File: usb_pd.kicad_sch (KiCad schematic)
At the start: 41 parts, among them J1 USB-C_GCT_USB4105-GF-A, J2 JST_SH_1x4_SM04B-SRSS-TB-LF-SN, Q1 SQS401EN-T1_BE3, U1 STUSB4500_QFN, U5 TVS2200DRVR, U6 TPD4E02B04DQA, U7 TVS2200DRVR, U8 TVS2200DRVR

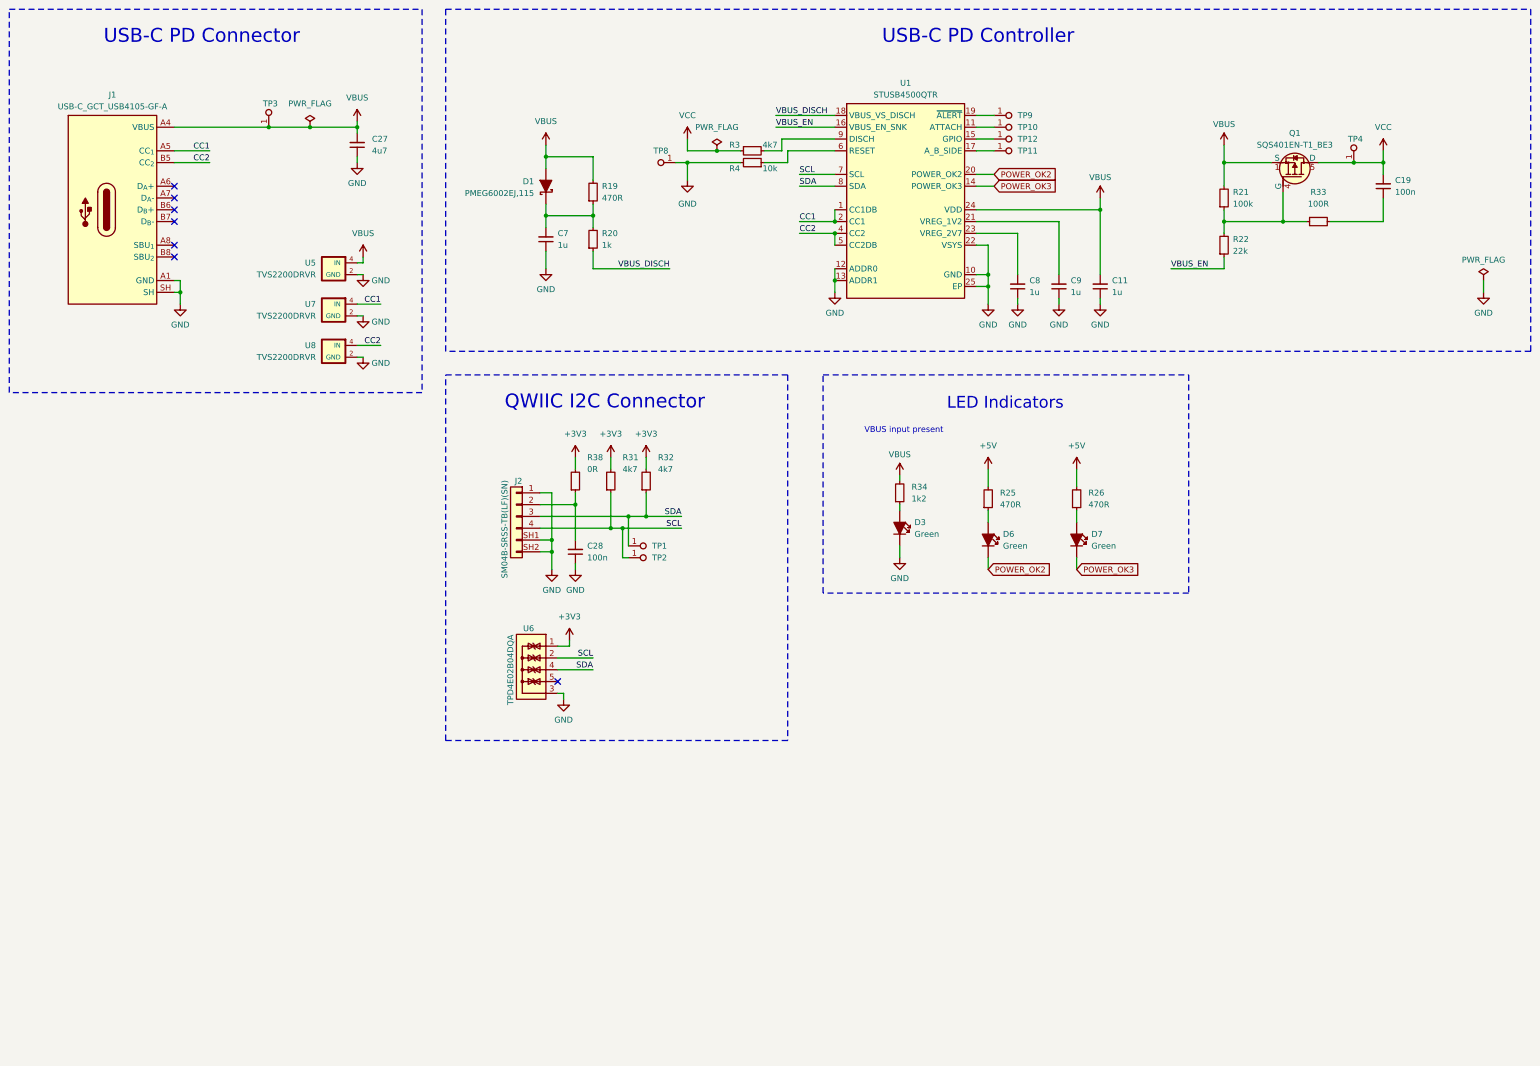
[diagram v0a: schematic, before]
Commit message: [#57225] Finish placement
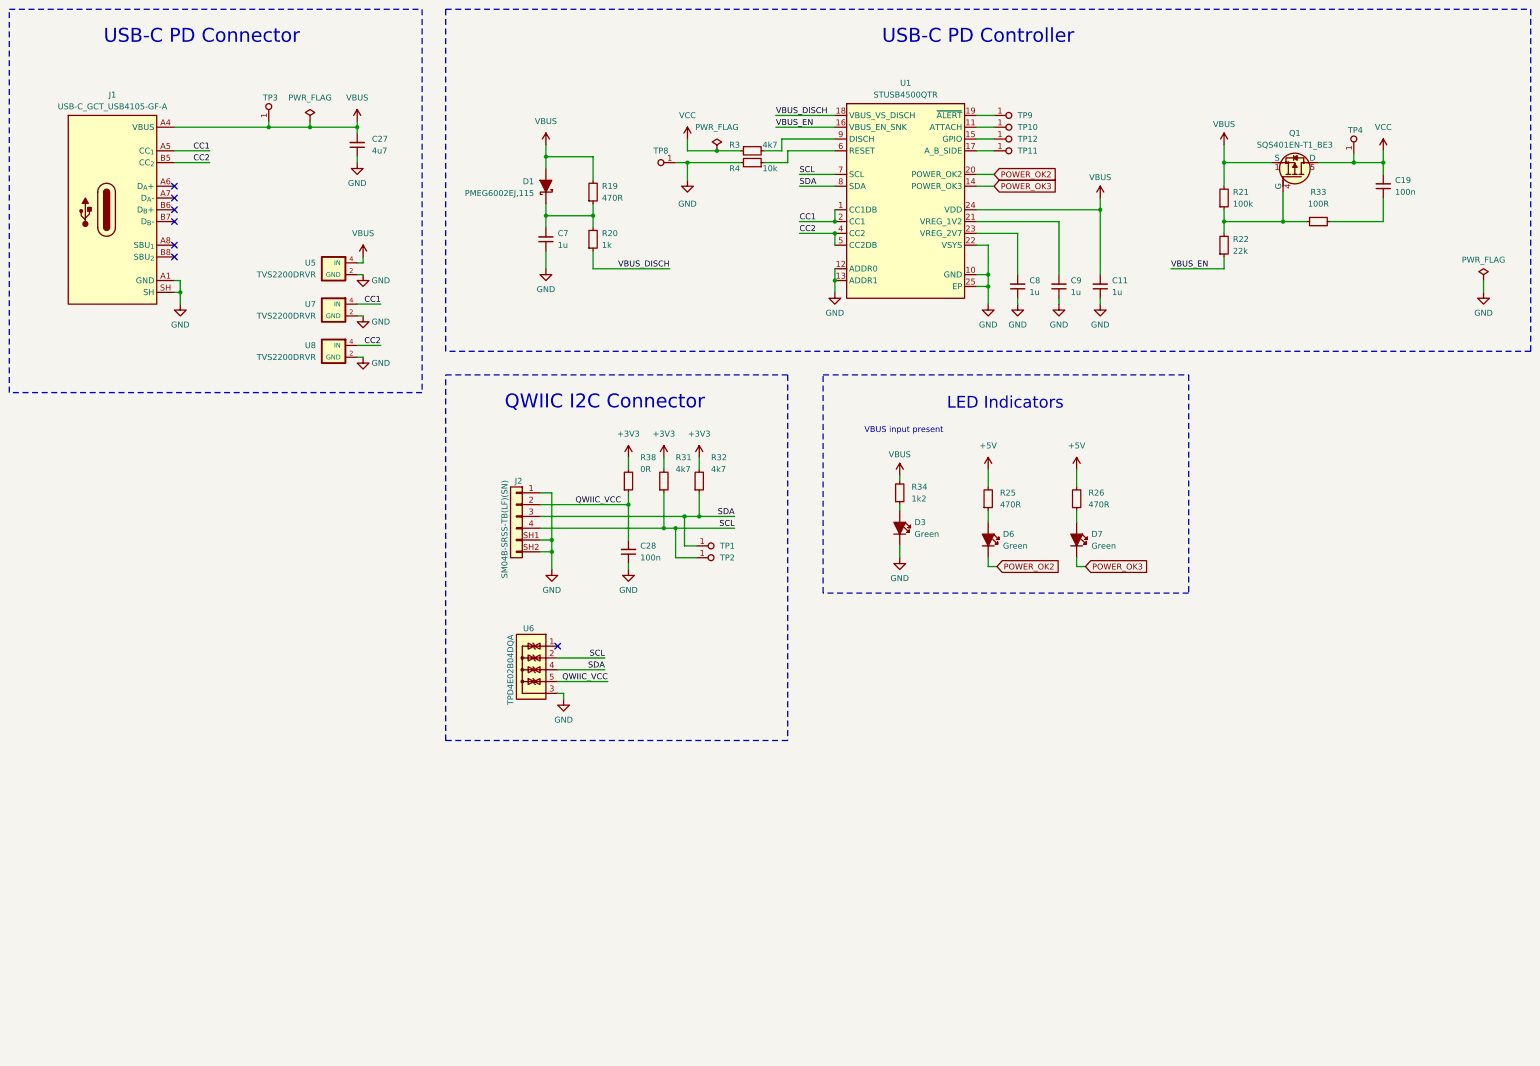
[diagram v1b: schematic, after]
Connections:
- net +3V3: no longer U6.1, U6.10
- net QWIIC_VCC: now reaches C28.2, J2.2, R38.1
- net QWIIC_VCC: now also U6.5, U6.6
- new net: U6.1, U6.10
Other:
- moved on the sheet: C28, R31, R32, R38, TP1, TP2, TP3, TP4

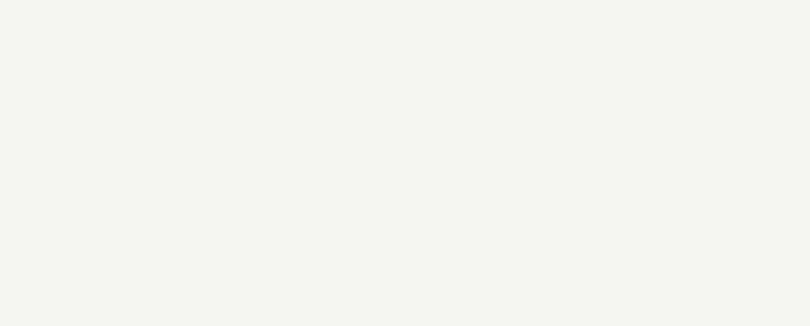
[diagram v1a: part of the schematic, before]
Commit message: [#57225] Add mounting pad
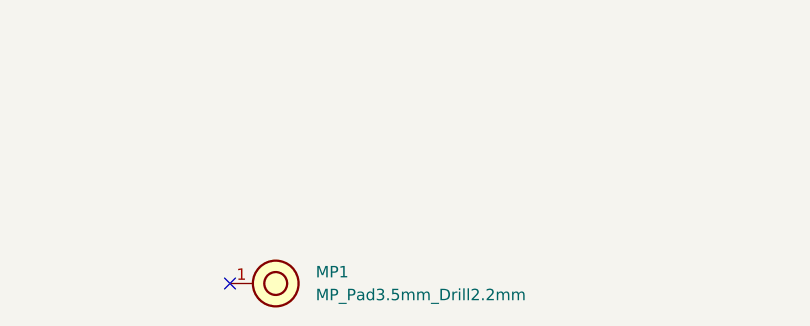
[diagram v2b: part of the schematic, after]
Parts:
- added MP1: MP_Pad3.5mm_Drill2.2mm, antmicro-footprints:MP_Pad3.5mm_Drill2.2mm, symbol antmicroMechanicalParts:MP_Pad3.5mm_Drill2.2mm
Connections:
- no-connect marks 7 -> 8
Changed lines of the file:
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@@
   )
   (no_connect (at 66.04 66.04))
+  (no_connect (at 107.315 250.825))
   (no_connect (at 66.04 78.74))
   (no_connect (at 148.59 165.1))
@@
         )
       )
+    )
+  )
+  (symbol (lib_id "antmicroMechanicalParts:MP_Pad3.5mm_Drill2.2mm") (at 107.315 250.825 0) (unit 1)
+    (in_bom no) (on_board yes) (dnp no) (fields_autoplaced)
+    (property "Reference" "MP1" (at 116.84 249.555 0)
+      (effects (font (size 1.27 1.27) (thickness 0.15)) (justify left))
+    )
+    (property "Value" "MP_Pad3.5mm_Drill2.2mm" (at 116.84 252.095 0)
+      (effects (font (size 1.27 1.27) (thickness 0.15)) (justify left))
+    )
+    (property "Footprint" "antmicro-footprints:MP_Pad3.5mm_Drill2.2mm" (at 122.555 260.985 0)
+      (effects (font (size 1.27 1.27) (thickness 0.15)) (justify left bottom) hide)
+    )
+    (property "Datasheet" "" (at 124.155 266.395 0)
+      (effects (font (size 1.27 1.27) (thickness 0.15)) (justify left bottom) hide)
+    )
+    (property "Author" "Antmicro" (at 122.555 266.065 0)
+      (effects (font (size 1.27 1.27) (thickness 0.15)) (justify left bottom) hide)
+    )
+    (property "License" "Apache-2.0" (at 122.555 268.605 0)
+      (effects (font (size 1.27 1.27) (thickness 0.15)) (justify left bottom) hide)
+    )
+    (pin "1")
+    (instances
+      (project "USB-C-power-adapter"
+        (path "/8da33aa8-79ed-467a-95ed-bf58aa0d1db6/344e016f-20ec-4e27-ac78-d9a1e9a3533b"
+          (reference "MP1") (unit 1)
+        )
+      )

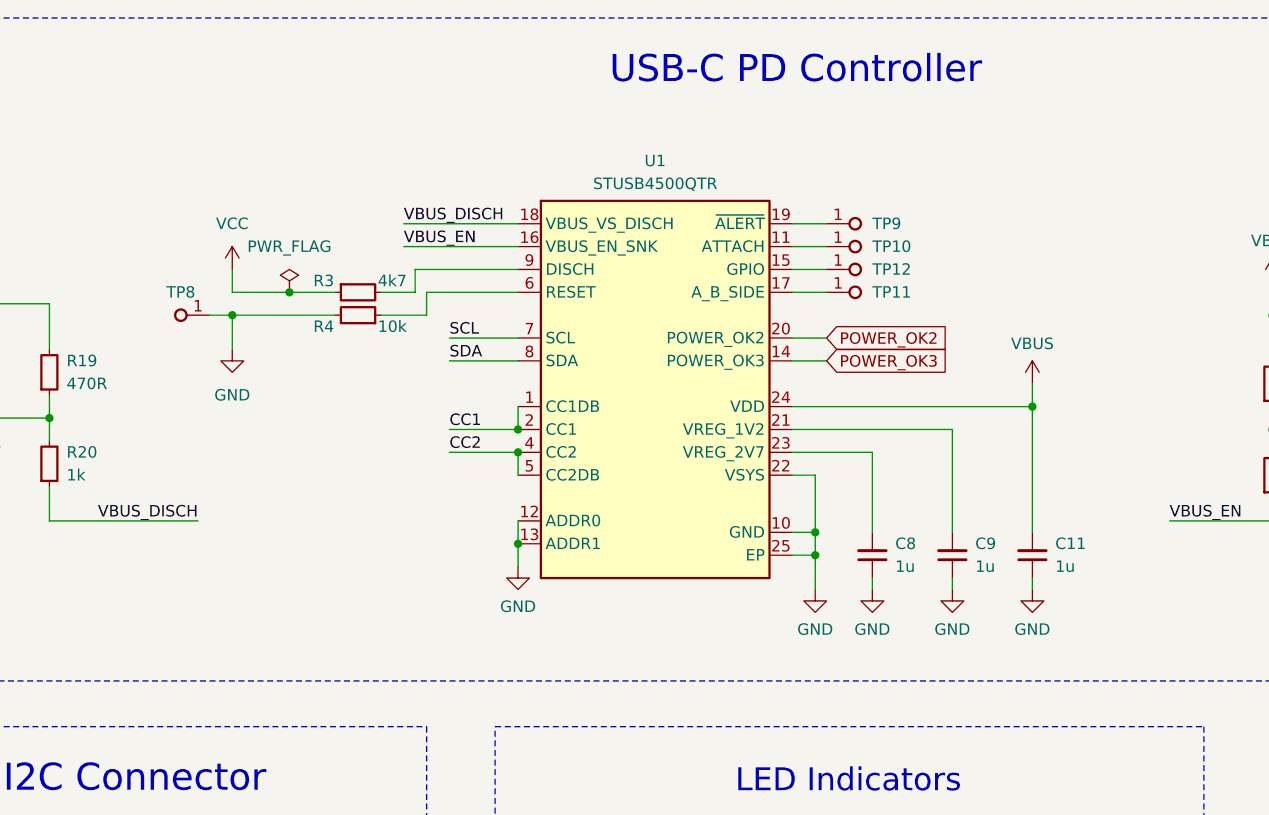
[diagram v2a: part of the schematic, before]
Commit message: [#57607] Update STUSB45 symbol
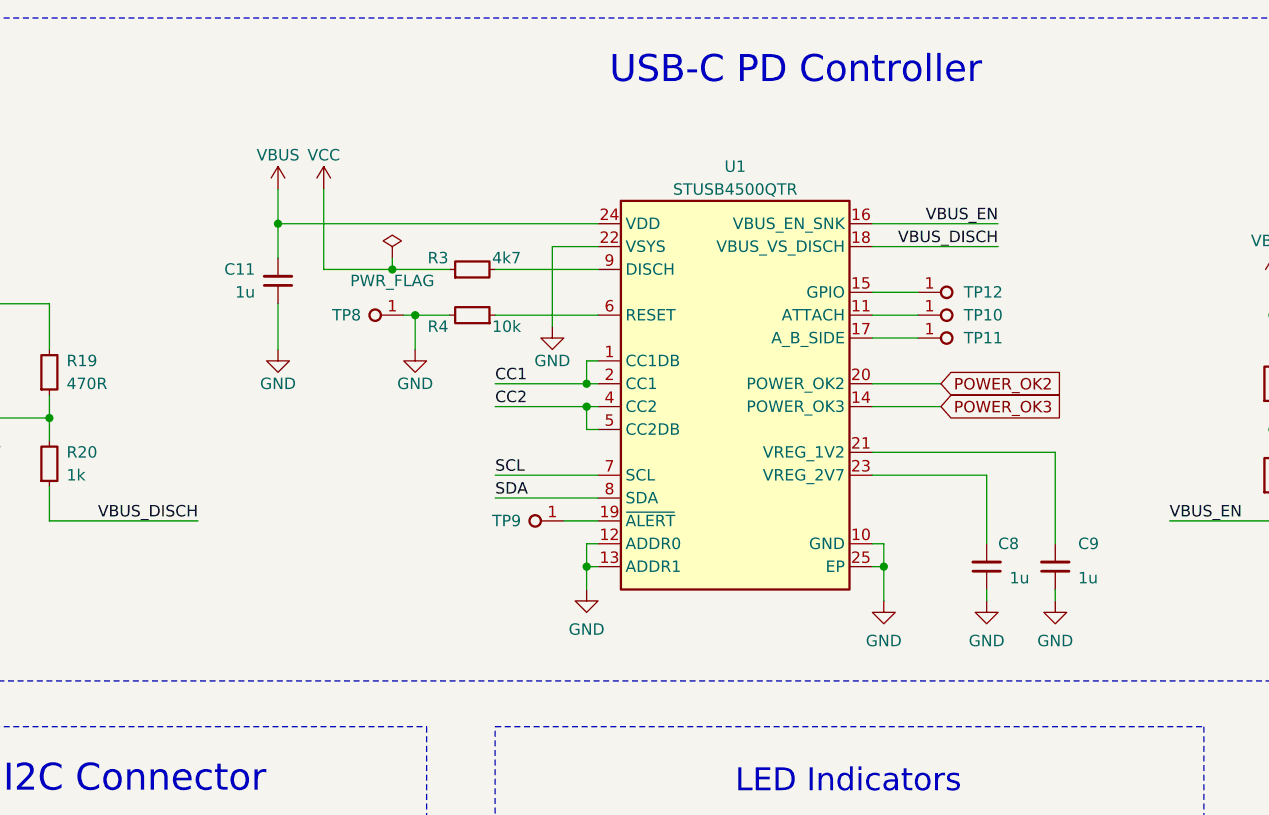
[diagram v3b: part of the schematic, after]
